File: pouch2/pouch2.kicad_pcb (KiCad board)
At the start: 2 copper layers, 80 x 100 mm, 142 parts, among them J101 Conn_01x06_Male, J102 Conn_01x03_Male, J103 Conn_01x04_Male, J501 Conn_01x02_Male, J502 Conn_01x02_Male, J503 Conn_01x02_Male, J504 Conn_01x02_Male, J701 PiZero, K701 AZ9371-1A-5DE, Q501 AO3401A, Q502 AO3401A, Q503 AO3401A, Q504 AO3401A, Q701 MMBT3906, SW501 SW_SPDT, SW801 SW_DIP_x08, U101 Pico, U201 BME688, U202 BME280, U901 SIM868

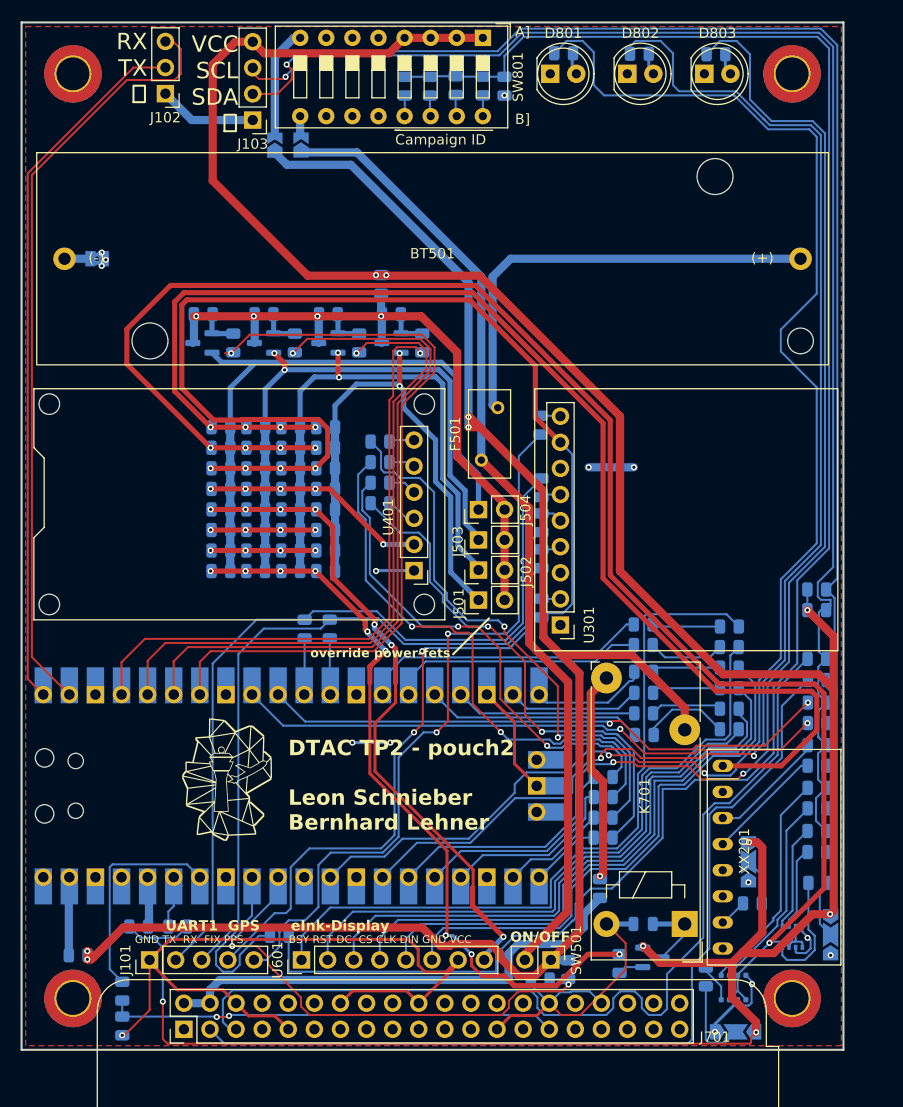
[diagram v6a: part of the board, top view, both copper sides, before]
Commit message: updated power routing
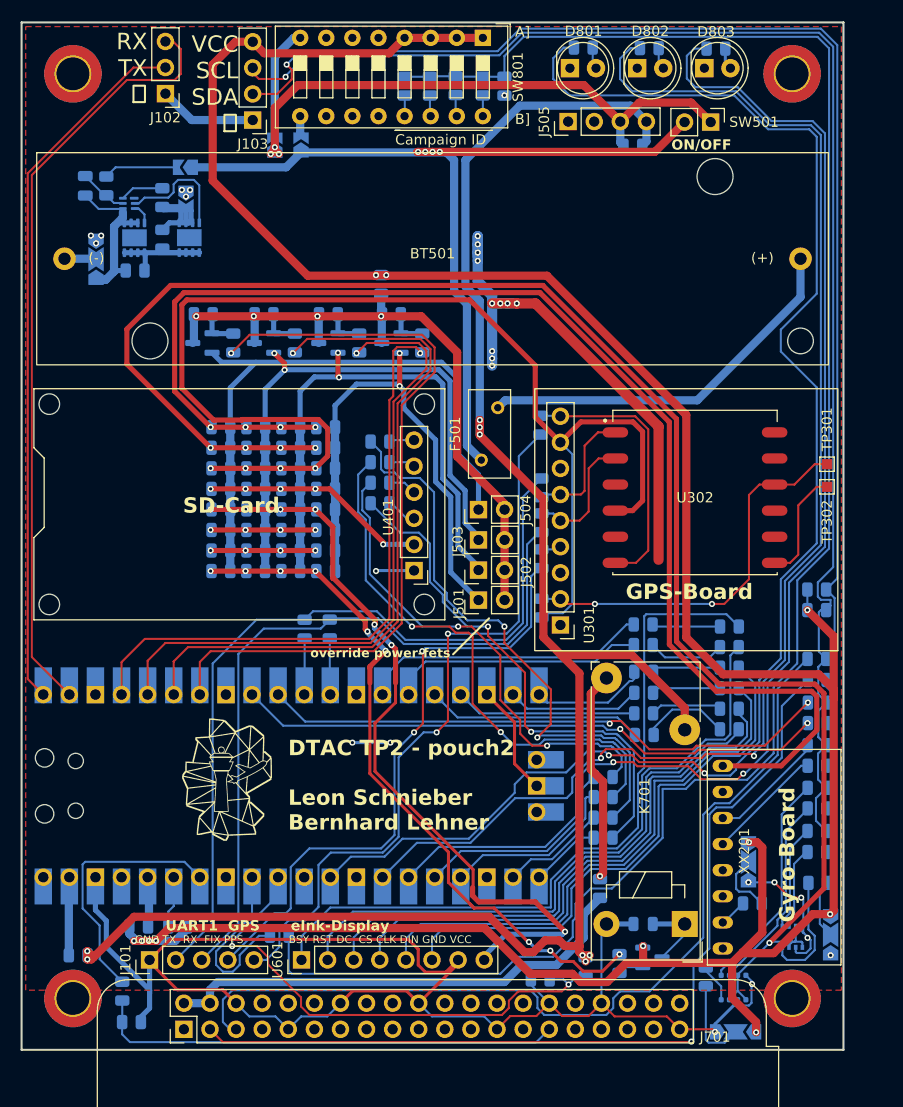
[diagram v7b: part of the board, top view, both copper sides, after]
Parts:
- removed JP501: Jumper_2_Bridged, Jumper:SolderJumper-2_P1.3mm_Bridged2Bar_Pad1.0x1.5mm
- added C501: 100n, Capacitor_SMD:C_0805_2012Metric, B.Cu at (56.2, 65.9)
- added J505: Conn_02x02_Odd_Even, Connector_PinHeader_2.54mm:PinHeader_1x04_P2.54mm_Vertical, F.Cu at (103.2, 59.6)
- added JP504: SolderJumper_3_Open, Jumper:SolderJumper-3_P2.0mm_Open_TrianglePad1.0x1.5mm_NumberLabels, B.Cu at (57.2, 73.0)
- added JP506: SolderJumper_2_Open, Jumper:SolderJumper-2_P1.3mm_Open_TrianglePad1.0x1.5mm, B.Cu at (66.0, 64.1)
- added JP507: SolderJumper_2_Open, Jumper:SolderJumper-2_P1.3mm_Open_TrianglePad1.0x1.5mm, B.Cu at (66.0, 67.1)
- added Q505: CSD16406Q3, Package_SON:VSON-8-1EP_3x3mm_P0.65mm_EP1.65x2.4mm, B.Cu at (66.3, 71.0)
- added Q506: CSD16406Q3, Package_SON:VSON-8-1EP_3x3mm_P0.65mm_EP1.65x2.4mm, B.Cu at (61.0, 71.0)
- added R542: 0, Resistor_SMD:R_0805_2012Metric, B.Cu at (109.5, 62.0)
- added R543: 2k2, Resistor_SMD:R_0805_2012Metric, B.Cu at (63.7, 67.0)
- added R544: 5M, Resistor_SMD:R_0805_2012Metric, B.Cu at (63.7, 71.1)
- added R545: 5M, Resistor_SMD:R_0805_2012Metric, B.Cu at (61.0, 74.2)
- added R546: 330, Resistor_SMD:R_0805_2012Metric, B.Cu at (58.2, 65.9)
- added TP301: TestPoint, TestPoint:TestPoint_Pad_1.0x1.0mm, F.Cu at (128.4, 93.0)
- added TP302: TestPoint, TestPoint:TestPoint_Pad_1.0x1.0mm, F.Cu at (128.4, 95.2)
- added U302: L86-M33, L86:XCVR_L86-M33, F.Cu at (115.5, 96.2)
- added U501: BQ29705, Package_SON:WSON-6_1.5x1.5mm_P0.5mm, B.Cu at (60.4, 67.6)
- BT501: value Battery_Cell -> XCell N18650CP-35E
- moved SW501 83.0 mm to (117.1, 59.7)
- moved D801 1.99 mm to (103.4, 54.5)
- moved R801 1.99 mm to (104.7, 52.5)
- moved R116 1.73 mm to (104.9, 141.9)
- moved D802 1.11 mm to (109.9, 54.5)
- moved R802 1.11 mm to (111.1, 52.5)
- moved R705 0.98 mm to (60.7, 147.3), turned to 0 degrees
- moved R803 0.55 mm to (117.6, 52.5)
- moved D803 0.55 mm to (116.5, 54.5)
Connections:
- JP502 pad 1: +BATT -> /Power/VCC_ANTE_BOOST
- K701 pad 11: +BATT -> VCC
- R113 pad 1: +BATT -> VCC
- R116 pad 1: +BATT -> VCC
- SW501 pad 1: +BATT -> /Power/VCC_ANTE_BOOST
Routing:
- net VCC: track 0.00 -> 178.8 mm, vias 0 -> 8
- net +BATT: track 167.6 -> 0.00 mm, vias 4 -> 0
- net GND: track 152.3 -> 238.9 mm, vias 15 -> 28
- net /Power/VCC_ANTE_BOOST: track 0.00 -> 54.2 mm, vias 0 -> 3
- net Net-(U301-EN): track 2.07 -> 38.6 mm, vias 0 -> 2
- net Net-(U301-PPS): track 2.01 -> 26.5 mm
- net /VCC_S3: track 104.0 -> 122.4 mm
- net Net-(JP504-A): track 0.00 -> 16.0 mm
- net Net-(Q505-D): track 0.00 -> 13.0 mm
- net Net-(Q505-G): track 0.00 -> 11.6 mm
- net /VCC_S5: track 64.2 -> 75.2 mm
- net Net-(U302-FORCE_ON): track 0.00 -> 11.0 mm
- net Net-(JP507-B): track 0.00 -> 10.8 mm
- net Net-(JP503-A): track 94.3 -> 83.9 mm, vias 0 -> 4
- net Net-(U301-RX): track 1.76 -> 12.1 mm
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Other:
- board text added: "GPS-Board"
- board text added: "Gyro-Board"
- board text added: "SD-Card"

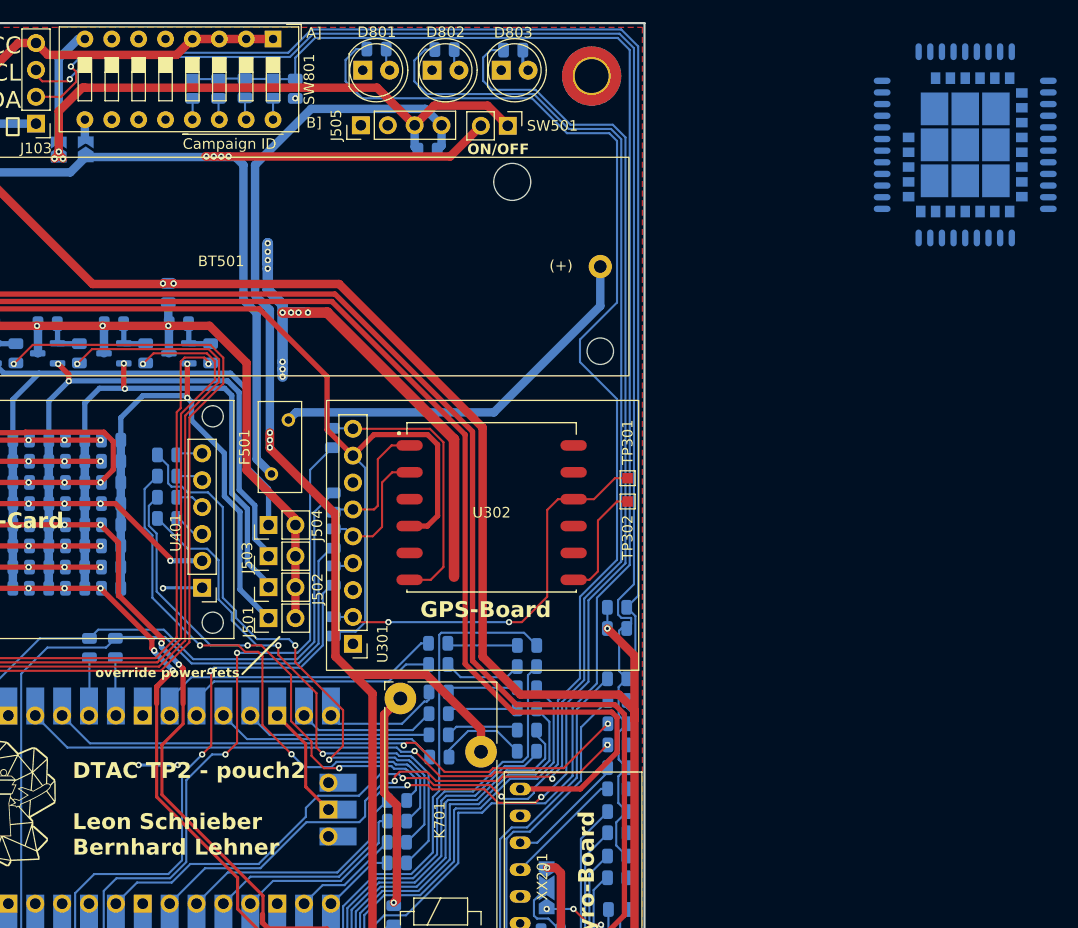
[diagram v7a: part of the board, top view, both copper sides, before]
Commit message: added sim-module breakout
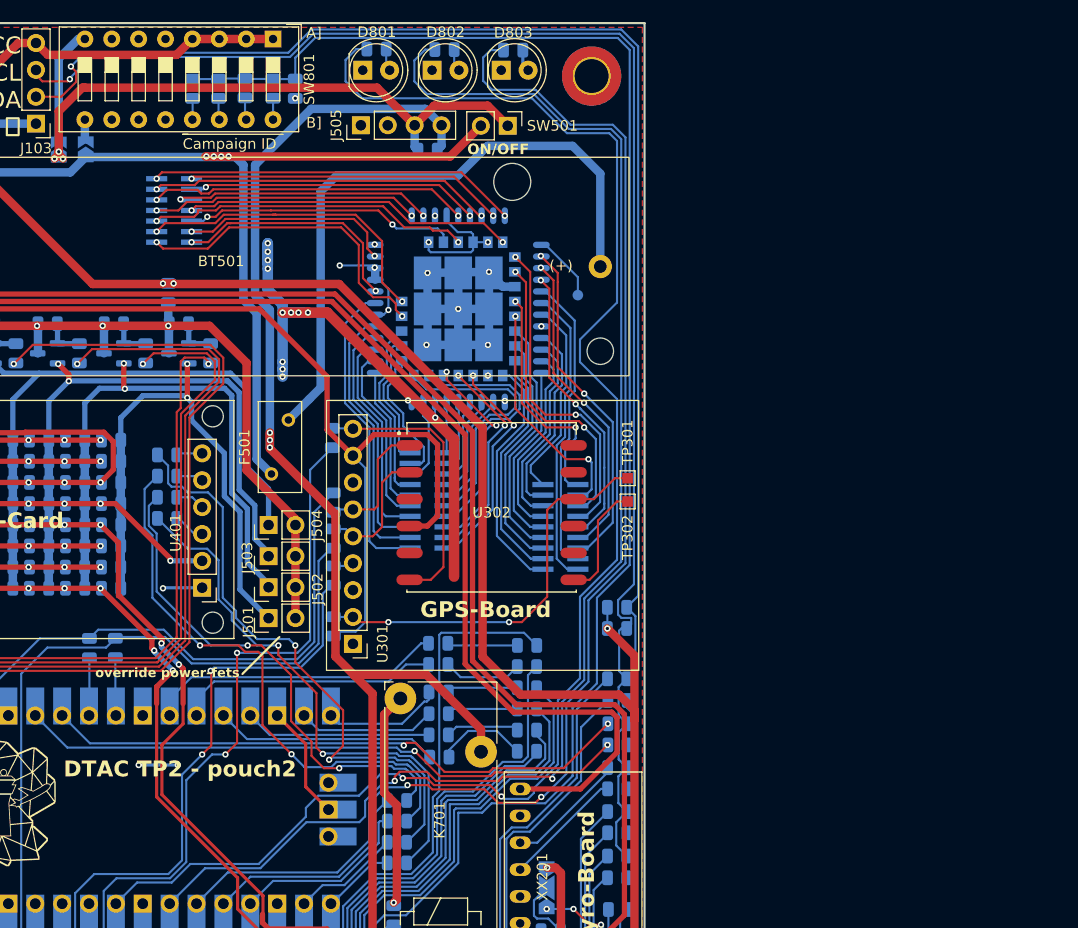
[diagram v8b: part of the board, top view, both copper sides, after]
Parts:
- added J901: Conn_02x03_Counter_Clockwise, Connector_PinHeader_1.00mm:PinHeader_2x10_P1.00mm_Vertical_SMD, B.Cu at (109.5, 95.1)
- added J902: Conn_02x07_Counter_Clockwise, Connector_PinHeader_1.00mm:PinHeader_2x07_P1.00mm_Vertical_SMD, B.Cu at (85.5, 67.7)
- added J903: Conn_02x09_Counter_Clockwise, Connector_PinHeader_1.00mm:PinHeader_2x09_P1.00mm_Vertical_SMD, B.Cu at (122.0, 97.6)
- added TP901: TestPoint, TestPoint:TestPoint_Pad_D1.0mm, B.Cu at (123.7, 75.7)
- moved U901 50.3 mm to (112.4, 77.0)
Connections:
- U901 pad 1: unconnected-(U901-UART1_TXD-Pad1) -> Net-(U901-UART1_TXD)
- U901 pad 10: unconnected-(U901-MICN-Pad10) -> Net-(J903-Pin_6)
- U901 pad 11: unconnected-(U901-SPK1P-Pad11) -> Net-(J903-Pin_8)
- U901 pad 12: unconnected-(U901-SPK1N-Pad12) -> Net-(J903-Pin_10)
- U901 pad 13: Net-(U901-GND-Pad13) -> GND
- U901 pad 14: unconnected-(U901-SIM1_DET-Pad14) -> Net-(J901-Pin_9)
- U901 pad 15: unconnected-(U901-SIM1_DATA-Pad15) -> Net-(J901-Pin_7)
- U901 pad 16: unconnected-(U901-SIM1_CLK-Pad16) -> Net-(J901-Pin_5)
- U901 pad 17: unconnected-(U901-SIM1_RST-Pad17) -> Net-(J901-Pin_3)
- U901 pad 18: unconnected-(U901-SIM1_VDD-Pad18) -> Net-(J901-Pin_1)
- U901 pad 19: Net-(U901-GND-Pad13) -> GND
- U901 pad 2: unconnected-(U901-UART1_RXD-Pad2) -> Net-(J903-Pin_13)
- U901 pad 20: unconnected-(U901-BT_ANT-Pad20) -> Net-(J901-Pin_6)
- U901 pad 21: Net-(U901-GND-Pad13) -> GND
- U901 pad 22: unconnected-(U901-UART2_TXD-Pad22) -> Net-(J901-Pin_10)
- U901 pad 23: unconnected-(U901-UART2_RXD-Pad23) -> Net-(J901-Pin_12)
- U901 pad 24: unconnected-(U901-USB_VBUS-Pad24) -> Net-(J901-Pin_14)
- U901 pad 25: unconnected-(U901-USB_DP-Pad25) -> Net-(J901-Pin_16)
- U901 pad 26: unconnected-(U901-USB_DM-Pad26) -> Net-(J901-Pin_18)
- U901 pad 27: Net-(U901-GND-Pad13) -> GND
- U901 pad 28: unconnected-(U901-VRTC-Pad28) -> Net-(J901-Pin_20)
- U901 pad 29: unconnected-(U901-RF_SYNC-Pad29) -> Net-(J902-Pin_13)
- U901 pad 3: unconnected-(U901-UART1_RTS-Pad3) -> Net-(J903-Pin_11)
- U901 pad 30: Net-(U901-GND-Pad13) -> GND
- U901 pad 31: Net-(U901-GND-Pad13) -> GND
- U901 pad 32: unconnected-(U901-GSM_ANT-Pad32) -> Net-(J902-Pin_11)
- U901 pad 33: Net-(U901-GND-Pad13) -> GND
- U901 pad 34: unconnected-(U901-GPS_VBAT-Pad34) -> Net-(J902-Pin_8)
- U901 pad 35: unconnected-(U901-VBAT-Pad35) -> Net-(J902-Pin_5)
- U901 pad 36: Net-(U901-GND-Pad13) -> GND
- U901 pad 37: Net-(U901-GND-Pad13) -> GND
- U901 pad 38: unconnected-(U901-ADC-Pad38) -> Net-(J902-Pin_6)
- U901 pad 39: unconnected-(U901-PWRKEY-Pad39) -> Net-(J902-Pin_3)
- U901 pad 4: unconnected-(U901-UART1_CTS-Pad4) -> Net-(J903-Pin_9)
- U901 pad 40: unconnected-(U901-VDD_EXT-Pad40) -> Net-(J902-Pin_4)
- U901 pad 41: unconnected-(U901-NETLIGHT-Pad41) -> Net-(J902-Pin_1)
- U901 pad 42: unconnected-(U901-STATUS-Pad42) -> Net-(J902-Pin_2)
- U901 pad 43: unconnected-(U901-SPK2N-Pad43) -> Net-(J903-Pin_7)
- U901 pad 44: unconnected-(U901-SPK2P-Pad44) -> Net-(J903-Pin_5)
- U901 pad 45: Net-(U901-GND-Pad13) -> GND
- U901 pad 46: unconnected-(U901-MCCA3-Pad46) -> Net-(J903-Pin_1)
- U901 pad 47: unconnected-(U901-MCCA2-Pad47) -> Net-(J903-Pin_3)
- U901 pad 48: unconnected-(U901-MCCA1-Pad48) -> Net-(J903-Pin_12)
- U901 pad 49: unconnected-(U901-MCCA0-Pad49) -> Net-(J903-Pin_14)
- U901 pad 5: unconnected-(U901-UART1_DCD-Pad5) -> Net-(J903-Pin_15)
- U901 pad 50: unconnected-(U901-MCCK-Pad50) -> Net-(J903-Pin_16)
- U901 pad 51: unconnected-(U901-MCCM0-Pad51) -> Net-(J903-Pin_18)
- U901 pad 53: unconnected-(U901-SIM2_DATA-Pad53) -> Net-(J901-Pin_19)
- U901 pad 54: unconnected-(U901-SIM2_CLK-Pad54) -> Net-(J901-Pin_17)
- U901 pad 55: unconnected-(U901-SIM2_RST-Pad55) -> Net-(J901-Pin_15)
- U901 pad 56: unconnected-(U901-SIM2_VDD-Pad56) -> Net-(J901-Pin_13)
- U901 pad 57: unconnected-(U901-GPIO1-Pad57) -> Net-(J901-Pin_11)
- U901 pad 58: unconnected-(U901-GPIO2-Pad58) -> Net-(J901-Pin_4)
- U901 pad 59: unconnected-(U901-GNSS_EN-Pad59) -> Net-(J901-Pin_2)
- U901 pad 6: unconnected-(U901-UART1_DTR-Pad6) -> Net-(J903-Pin_17)
- U901 pad 60: unconnected-(U901-1PPS-Pad60) -> Net-(J901-Pin_8)
- U901 pad 61: unconnected-(U901-GPS_TXD-Pad61) -> Net-(J902-Pin_14)
- U901 pad 62: unconnected-(U901-GPS_RXD-Pad62) -> Net-(J902-Pin_12)
- U901 pad 63: Net-(U901-GND-Pad13) -> GND
- U901 pad 64: unconnected-(U901-SDA-Pad64) -> Net-(J902-Pin_9)
- U901 pad 65: unconnected-(U901-SCL-Pad65) -> Net-(J902-Pin_10)
- U901 pad 66: Net-(U901-GND-Pad13) -> GND
- U901 pad 67: Net-(U901-GND-Pad13) -> GND
- U901 pad 68: unconnected-(U901-GPS_ANT-Pad68) -> Net-(J902-Pin_7)
- U901 pad 69: Net-(U901-GND-Pad13) -> GND
- U901 pad 7: unconnected-(U901-UART1_RI-Pad7) -> Net-(J903-Pin_2)
- U901 pad 70: Net-(U901-GND-Pad13) -> GND
- U901 pad 71: Net-(U901-GND-Pad13) -> GND
- U901 pad 72: Net-(U901-GND-Pad13) -> GND
- U901 pad 73: Net-(U901-GND-Pad13) -> GND
- U901 pad 74: Net-(U901-GND-Pad13) -> GND
- U901 pad 75: Net-(U901-GND-Pad13) -> GND
- U901 pad 76: Net-(U901-GND-Pad13) -> GND
- U901 pad 77: Net-(U901-GND-Pad13) -> GND
- U901 pad 8: Net-(U901-GND-Pad13) -> GND
- U901 pad 9: unconnected-(U901-MICP-Pad9) -> Net-(J903-Pin_4)
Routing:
- net GND: track 238.9 -> 304.1 mm, vias 28 -> 44
- net Net-(J902-Pin_2): track 0.00 -> 34.9 mm, vias 0 -> 2
- net Net-(J902-Pin_4): track 0.00 -> 32.4 mm, vias 0 -> 2
- net Net-(J903-Pin_13): track 0.00 -> 32.3 mm, vias 0 -> 2
- net Net-(J902-Pin_7): track 0.00 -> 31.3 mm, vias 0 -> 2
- net Net-(J903-Pin_7): track 0.00 -> 31.1 mm, vias 0 -> 2
- net Net-(J902-Pin_10): track 0.00 -> 30.7 mm, vias 0 -> 2
- net Net-(J902-Pin_6): track 0.00 -> 30.2 mm, vias 0 -> 2
- net Net-(J902-Pin_14): track 0.00 -> 30.2 mm, vias 0 -> 2
- net Net-(J902-Pin_1): track 0.00 -> 30.1 mm, vias 0 -> 2
- net Net-(J903-Pin_11): track 0.00 -> 29.8 mm, vias 0 -> 2
- net Net-(J902-Pin_12): track 0.00 -> 29.8 mm, vias 0 -> 2
- net Net-(J901-Pin_20): track 0.00 -> 29.3 mm
- net Net-(J903-Pin_17): track 0.00 -> 28.5 mm
- net Net-(J903-Pin_15): track 0.00 -> 28.4 mm
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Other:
- board text added: "DTAC TP2 - pouch2"
- board text removed: "DTAC TP2 - pouch2 Leon Schnieber Bernhard Lehner"
